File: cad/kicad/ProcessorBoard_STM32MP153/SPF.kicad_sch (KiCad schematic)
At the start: 65 parts, among them J501 SFP, U501 DSC6101HL3B-025.0000, U502 TXS0102DCU, U503 SN74LVC07AD, U504 SN74LVC07AD, X501 RTL8211FS(I)-xx-xx

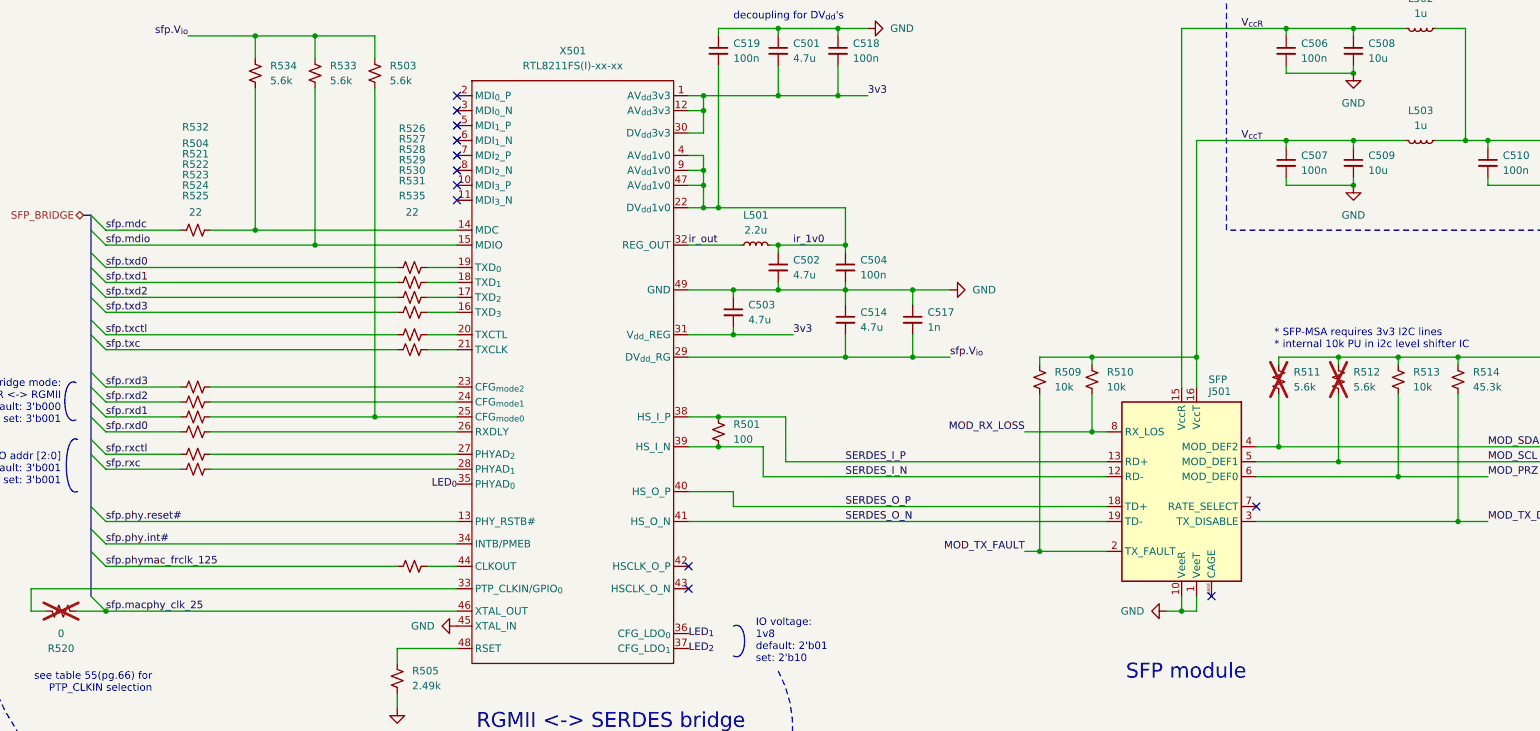
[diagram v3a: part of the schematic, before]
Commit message: more traces. anything to avoid soldering
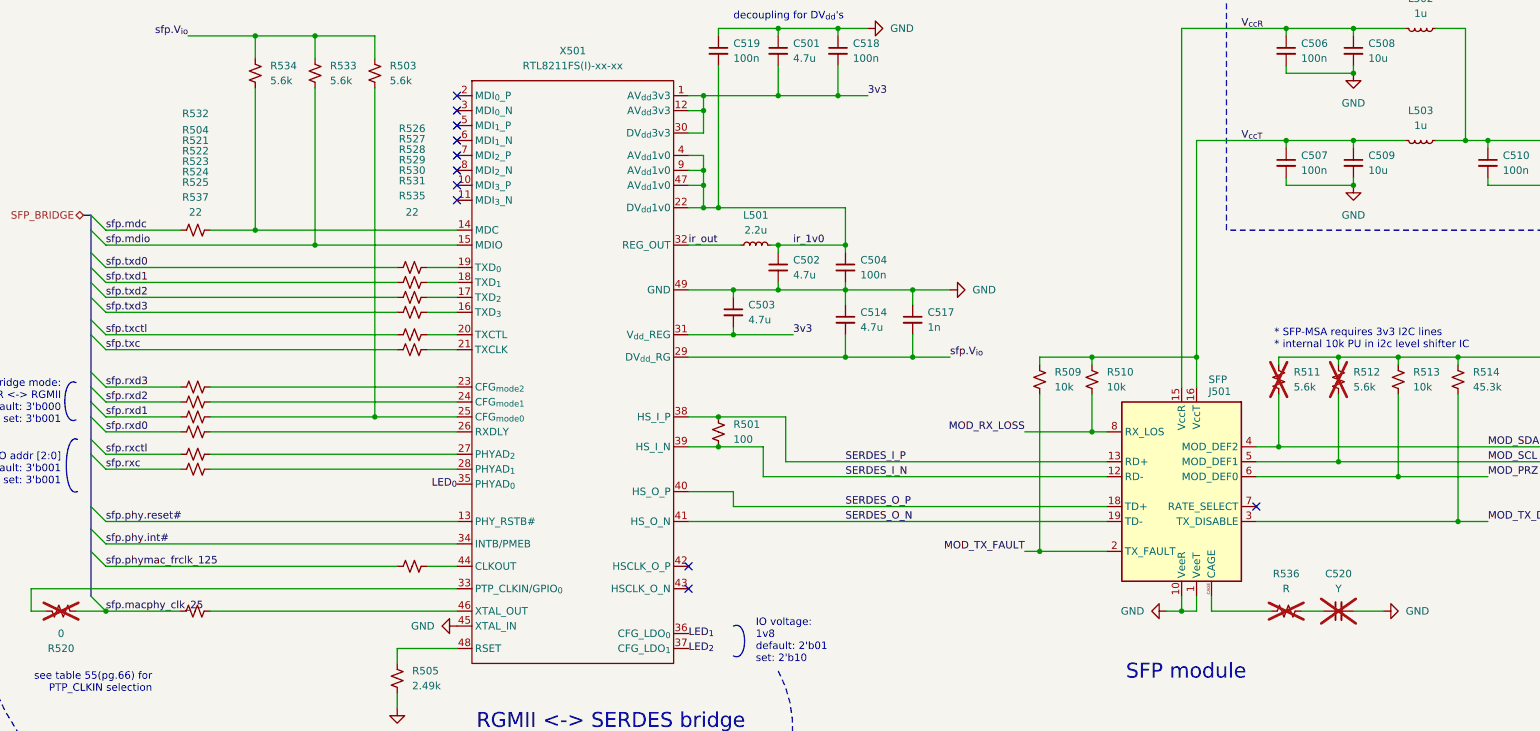
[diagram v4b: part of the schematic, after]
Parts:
- added C520: Y, Capacitor_SMD:C_0402_1005Metric_Pad0.74x0.62mm_HandSolder, symbol Device:C_Small
- added R536: R, Resistor_SMD:R_0603_1608Metric, symbol Device:R_Small_US
- added R537: 22, Resistor_SMD:R_0603_1608Metric, symbol Device:R_Small_US
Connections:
- net GND: now also C520.2
- net sfp.macphy_clk_25: now also R537.1; no longer X501.46 (XTAL_OUT)
- net at J501.CAGE: now also R536.1
- new net: R537.2, X501.46 (XTAL_OUT)
- new net: C520.1, R536.2
- no-connect marks 13 -> 12

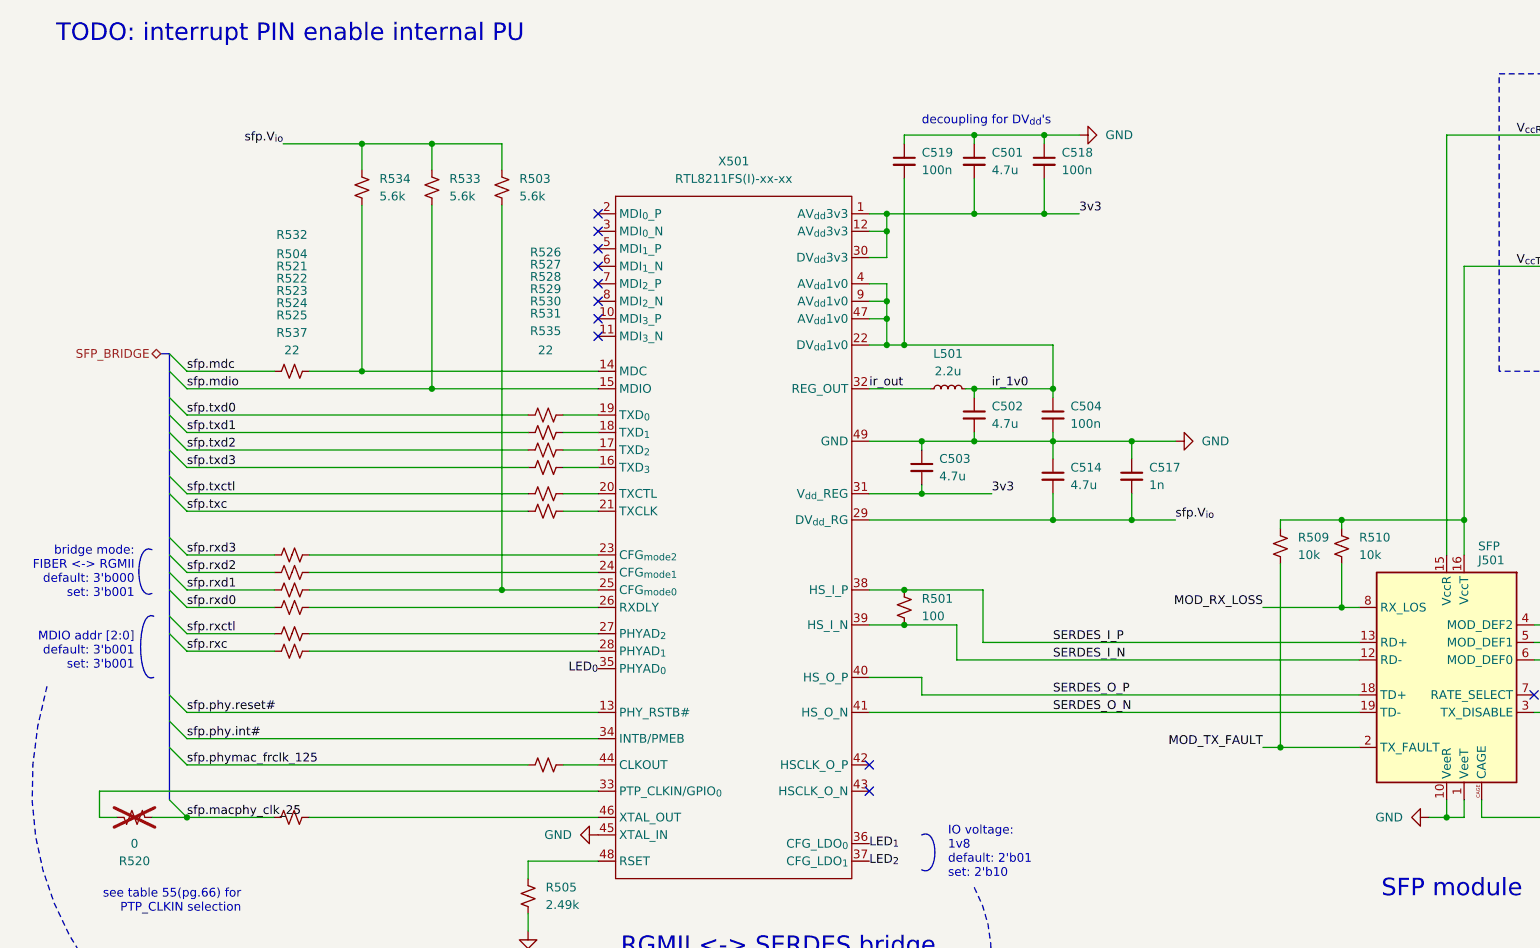
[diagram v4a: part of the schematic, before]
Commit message: shuffled core back to left side of board, fits better
row row the power planes under mpu
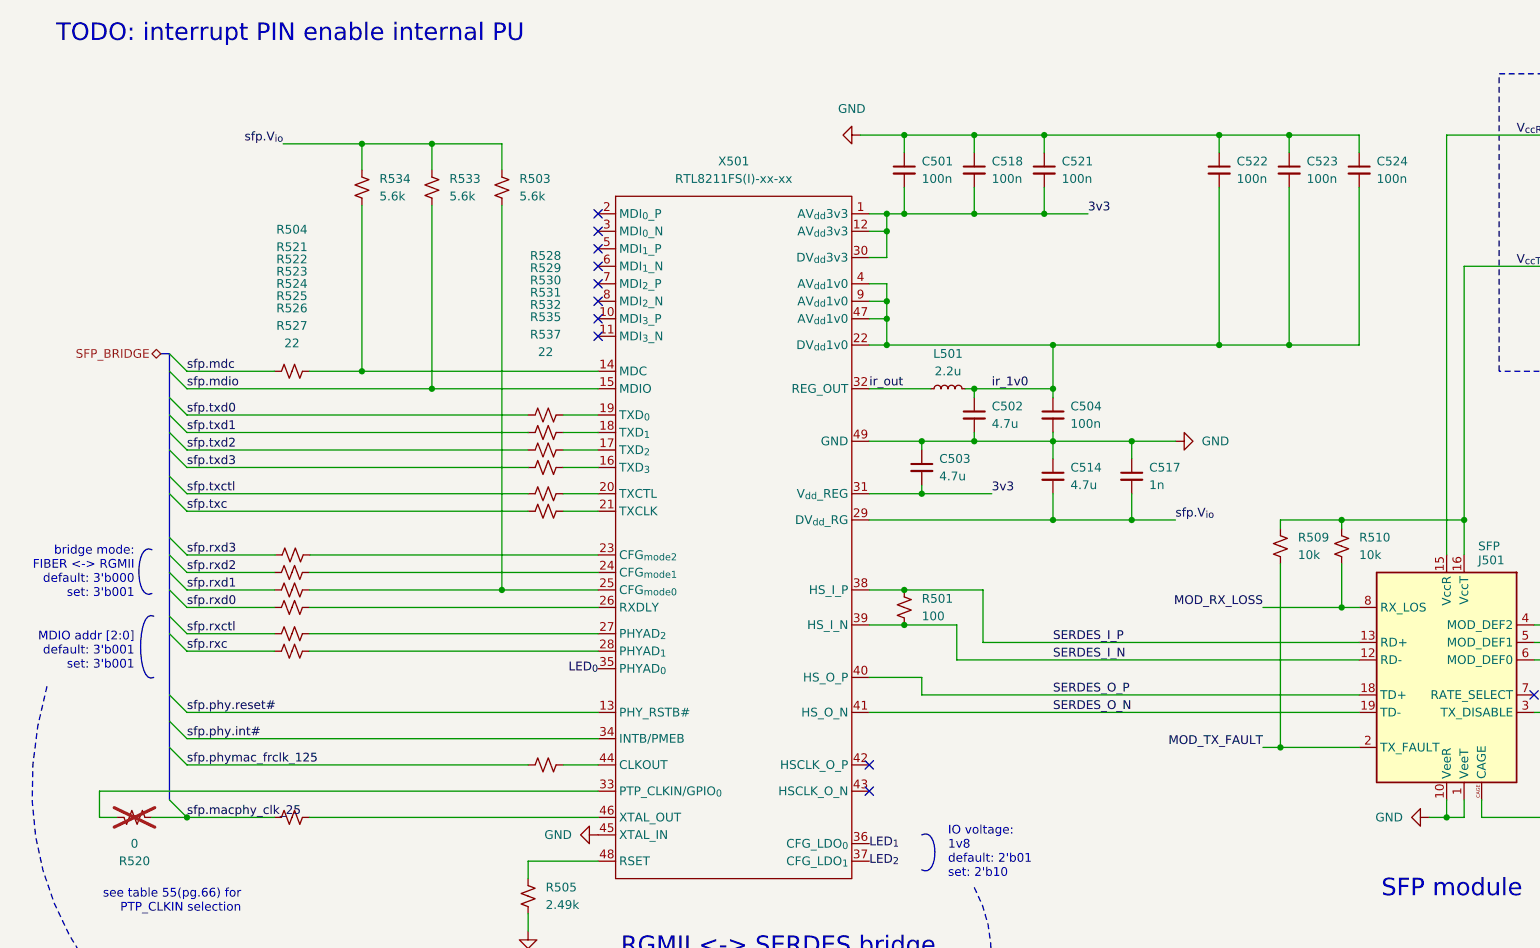
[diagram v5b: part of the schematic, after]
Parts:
- removed C519: 100n, Capacitor_SMD:C_0402_1005Metric_Pad0.74x0.62mm_HandSolder, symbol Device:C_Small
- added C521, C522, C523, C524: 100n, Capacitor_SMD:C_0402_1005Metric_Pad0.74x0.62mm_HandSolder, symbol Device:C_Small
- C501: value 4.7u -> 100n; character https://ds.murata.com/simsurfing/mlcc.html?partnumbers=%5B%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 -> http://ksim.kemet.com/?pn=C0402C104K4PAC7411&disty=mouser; mouser https://www.mouser.com/en/ProductDetail/Murata-Electronics/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 -> https://www.mouser.com/en/ProductDetail/KEMET/C0402C104K4PA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; unit x1 0.047 -> 0.10; unit x10 0.11 -> 0.048
- R504, R521, R522, R523, R524, R525, R526, R527, R528, R529, R530, R531, R532, R535, R537: footprint Resistor_SMD:R_0603_1608Metric -> Resistor_SMD:R_0402_1005Metric_Pad0.72x0.64mm_HandSolder; mouser https://www.mouser.com/en/ProductDetail/YAGEO/RT0603DRE0722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 -> https://www.mouser.com/en/ProductDetail/Vishay/CRCW040222R0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; unit x10 0.018 -> 0.02; now in the parts list
- R520: footprint Resistor_SMD:R_0603_1608Metric -> Resistor_SMD:R_0402_1005Metric_Pad0.72x0.64mm_HandSolder
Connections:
- net 3v3: now also C521.2
- net GND: now also C521.1, C522.1, C523.1, C524.1
- net ir_1v0: now also C522.2, C523.2, C524.2
- net sfp.macphy_clk_25: now also R520.1, R527.1; no longer R520.2, R537.1
- net sfp.mdc: now also R504.1; no longer R532.1
- net sfp.phymac_frclk_125: now also R537.1; no longer R535.1
- net sfp.rxc: now also R526.1; no longer R525.1
- net sfp.rxctl: now also R525.1; no longer R524.1
- net sfp.rxd0: now also R524.1; no longer R523.1
- net sfp.rxd1: now also R523.1; no longer R522.1
- net sfp.rxd2: now also R522.1; no longer R521.1
- net sfp.rxd3: now also R521.1; no longer R504.1
- net sfp.txc: now also R535.1; no longer R531.1
- net sfp.txctl: now also R532.1; no longer R530.1
- net sfp.txd0: now also R528.1; no longer R526.1
- net sfp.txd1: now also R529.1; no longer R527.1
- net sfp.txd2: now also R530.1; no longer R528.1
- net sfp.txd3: now also R531.1; no longer R529.1
- net at X501.33 (PTP_CLKIN/GPIO_{0}): now also R520.2; no longer R520.1
- net at R529.2: now also X501.18 (TXD_{1}); no longer X501.16 (TXD_{3})
- net at R523.2: now also R503.2, X501.25 (CFG_{mode0}); no longer X501.26 (RXDLY)
- net at X501.27 (PHYAD_{2}): now also R525.2; no longer R524.2
- net at R528.2: now also X501.19 (TXD_{0}); no longer X501.17 (TXD_{2})
- net at R537.2: now also X501.44 (CLKOUT); no longer X501.46 (XTAL_OUT)
- net at R530.2: now also X501.17 (TXD_{2}); no longer X501.20 (TXCTL)
- net at R526.2: now also X501.28 (PHYAD_{1}); no longer X501.19 (TXD_{0})
- net at X501.24 (CFG_{mode1}): now also R522.2; no longer R521.2
- net at X501.21 (TXCLK): now also R535.2; no longer R531.2
- net at R534.2, X501.14 (MDC): now also R504.2; no longer R532.2
- net at X501.23 (CFG_{mode2}): now also R521.2; no longer R504.2
- net at R527.2: now also X501.46 (XTAL_OUT); no longer X501.18 (TXD_{1})
- new net: R531.2, X501.16 (TXD_{3})
- new net: R524.2, X501.26 (RXDLY)
- new net: R532.2, X501.20 (TXCTL)
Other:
- note removed: "decoupling for DV_{dd}'s"
- moved on the sheet: C518

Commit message: moners
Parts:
- added C519: 100n, Capacitor_SMD:C_0402_1005Metric_Pad0.74x0.62mm_HandSolder, symbol Device:C_Small
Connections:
- net GND: now also C519.1
- net ir_1v0: now also C519.2
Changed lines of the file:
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@@
 	)
 	(junction
+		(at 179.07 36.83)
+		(diameter 0)
+		(color 0 0 0 0)
+	)
+	(junction
+		(at 179.07 67.31)
+		(diameter 0)
+		(color 0 0 0 0)
+	)
+	(junction
 		(at 165.1 73.66)
 		(diameter 0)
@@
 	(wire
 		(pts
+			(xy 179.07 44.45) (xy 179.07 67.31)
+		)
+		(stroke
+			(width 0)
+			(type default)
+		)
+	)
+	(wire
+		(pts
 			(xy 209.55 44.45) (xy 209.55 67.31)
 		)
@@
 	(wire
 		(pts
-			(xy 163.83 36.83) (xy 189.23 36.83)
+			(xy 163.83 36.83) (xy 179.07 36.83)
 		)
 		(stroke
@@
 	(wire
 		(pts
+			(xy 179.07 67.31) (xy 189.23 67.31)
+		)
+		(stroke
+			(width 0)
+			(type default)
+		)
+	)
+	(wire
+		(pts
 			(xy 93.98 88.9) (xy 99.06 88.9)
 		)
@@
 	(wire
 		(pts
-			(xy 165.1 67.31) (xy 189.23 67.31)
+			(xy 165.1 67.31) (xy 179.07 67.31)
 		)
 		(stroke
@@
 	(wire
 		(pts
+			(xy 179.07 36.83) (xy 189.23 36.83)
+		)
+		(stroke
+			(width 0)
+			(type default)
+		)
+	)
+	(wire
+		(pts
 			(xy 105.41 227.33) (xy 113.03 227.33)
 		)
@@
 	(wire
 		(pts
+			(xy 179.07 36.83) (xy 179.07 39.37)
+		)
+		(stroke
+			(width 0)
+			(type default)
+		)
+	)
+	(wire
+		(pts
 			(xy 143.51 102.87) (xy 154.94 102.87)
 		)
@@
 					(unit 1)
 				)
+			)
+		)
+	)
+	(symbol
+		(lib_id "Device:C_Small")
+		(at 179.07 41.91 0)
+		(unit 1)
+		(body_style 1)
+		(exclude_from_sim no)
+		(in_bom yes)
+		(on_board yes)
+		(in_pos_files yes)
+		(dnp no)
+		(fields_autoplaced yes)
+		(property "Reference" "C519"
+			(at 181.61 40.6462 0)
+			(show_name no)
+			(do_not_autoplace no)
+			(effects
+				(font
+					(size 1.27 1.27)
+				)
+				(justify left)
+			)
+		)
+		(property "Value" "100n"
+			(at 181.61 43.1862 0)
+			(show_name no)
+			(do_not_autoplace no)
+			(effects
+				(font
+					(size 1.27 1.27)
+				)
+				(justify left)
+			)
+		)
+		(property "Footprint" "Capacitor_SMD:C_0402_1005Metric_Pad0.74x0.62mm_HandSolder"
+			(at 179.07 41.91 0)
+			(hide yes)
+			(show_name no)
+			(do_not_autoplace no)
+			(effects
+				(font
+					(size 1.27 1.27)
+				)
+			)
+		)
+		(property "Datasheet" ""
+			(at 179.07 41.91 0)
+			(hide yes)
+			(show_name no)
+			(do_not_autoplace no)
+			(effects
+				(font
+					(size 1.27 1.27)
+				)
+			)
+		)
+		(property "Description" "100nF, 10%, 16Vdc, 34MHz"
+			(at 179.07 41.91 0)
+			(hide yes)
+			(show_name no)
+			(do_not_autoplace no)
+			(effects
+				(font
+					(size 1.27 1.27)
+				)
+			)
+		)
+		(property "mouser" "https://www.mouser.com/en/ProductDetail/KEMET/C0402C104K4PAC7411?qs=sSYV1F9c5cGYoSNLRebUBQ%3D%3D"
+			(at 179.07 41.91 0)
+			(hide yes)
+			(show_name no)
+			(do_not_autoplace no)
+			(effects
+				(font
+					(size 1.27 1.27)
+				)
+			)
+		)
+		(property "unit x10" "0.048"
+			(at 179.07 41.91 0)
+			(hide yes)
+			(show_name no)
+			(do_not_autoplace no)
+			(effects
+				(font
+					(size 1.27 1.27)
+				)
+			)
+		)
+		(property "unit x1" "0.10"
+			(at 179.07 41.91 0)
+			(hide yes)
+			(show_name no)
+			(do_not_autoplace no)
+			(effects
+				(font
+					(size 1.27 1.27)
+				)
+			)
+		)
+		(property "character" "http://ksim.kemet.com/?pn=C0402C104K4PAC7411&disty=mouser"
+			(at 179.07 41.91 0)
+			(hide yes)
+			(show_name no)
+			(do_not_autoplace no)
+			(effects
+				(font
+					(size 1.27 1.27)
+				)
+			)
+		)
+		(property "Arrow Part Number" ""
+			(at 179.07 41.91 0)
+			(hide yes)
+			(show_name no)
+			(do_not_autoplace no)
+			(effects
+				(font
+					(size 1.27 1.27)
+				)
+			)
+		)
+		(property "Arrow Price/Stock" ""
+			(at 179.07 41.91 0)
+			(hide yes)
+			(show_name no)
+			(do_not_autoplace no)
+			(effects
+				(font
+					(size 1.27 1.27)
+				)
+			)
+		)
+		(pin "1"
+		)
+		(pin "2"
+		)
+		(instances
+			(project "ProcessorBoard_STM32MP153"
+				(path "/e63e39d7-6ac0-4ffd-8aa3-1841a4541b55/9bbfbe68-2804-40ed-9d5f-0570a6a580b2"
+					(reference "C519")
+					(unit 1)
+				)
